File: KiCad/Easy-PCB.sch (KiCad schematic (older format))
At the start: 0 parts

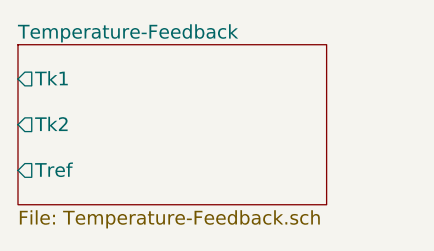
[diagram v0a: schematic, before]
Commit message: nichrome mounting parts added to bom and feedback terminal block removed
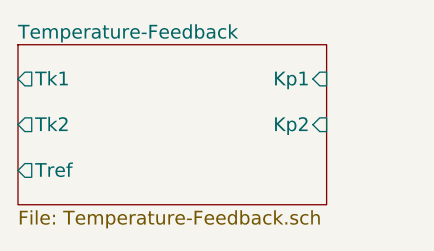
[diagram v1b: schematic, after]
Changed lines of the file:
@@
 F3 "Tk2" O L 4950 5600 60
 F4 "Tref" O L 4950 5800 60
+F5 "Kp1" I R 6300 5400 60
+F6 "Kp2" I R 6300 5600 60
 $EndSheet
 $EndSCHEMATC

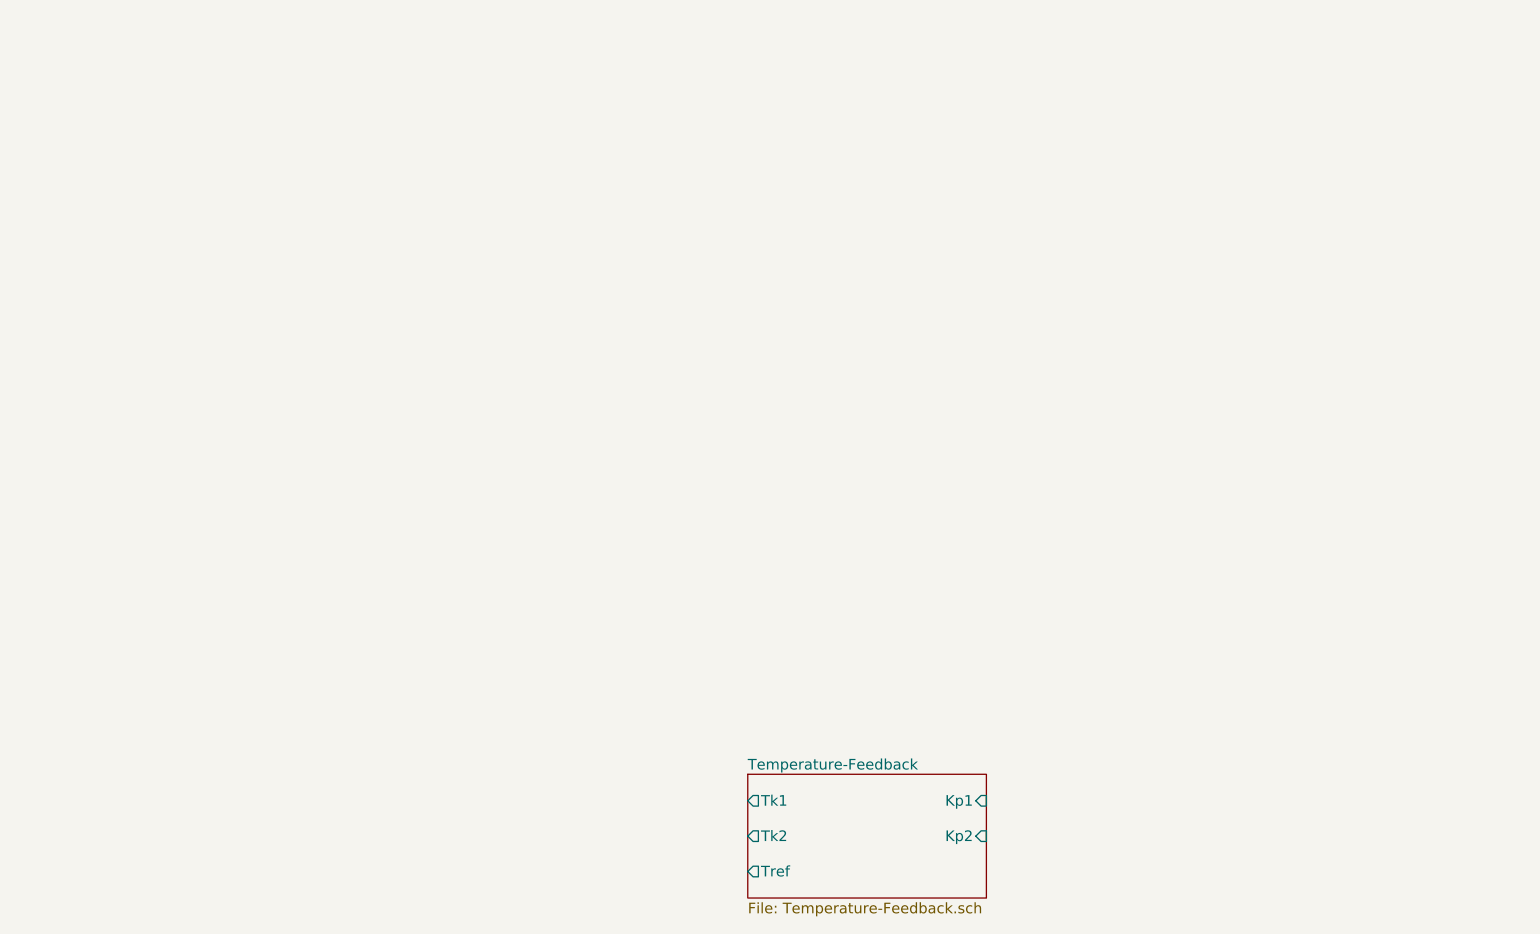
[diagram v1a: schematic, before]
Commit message: power circuit requirements section
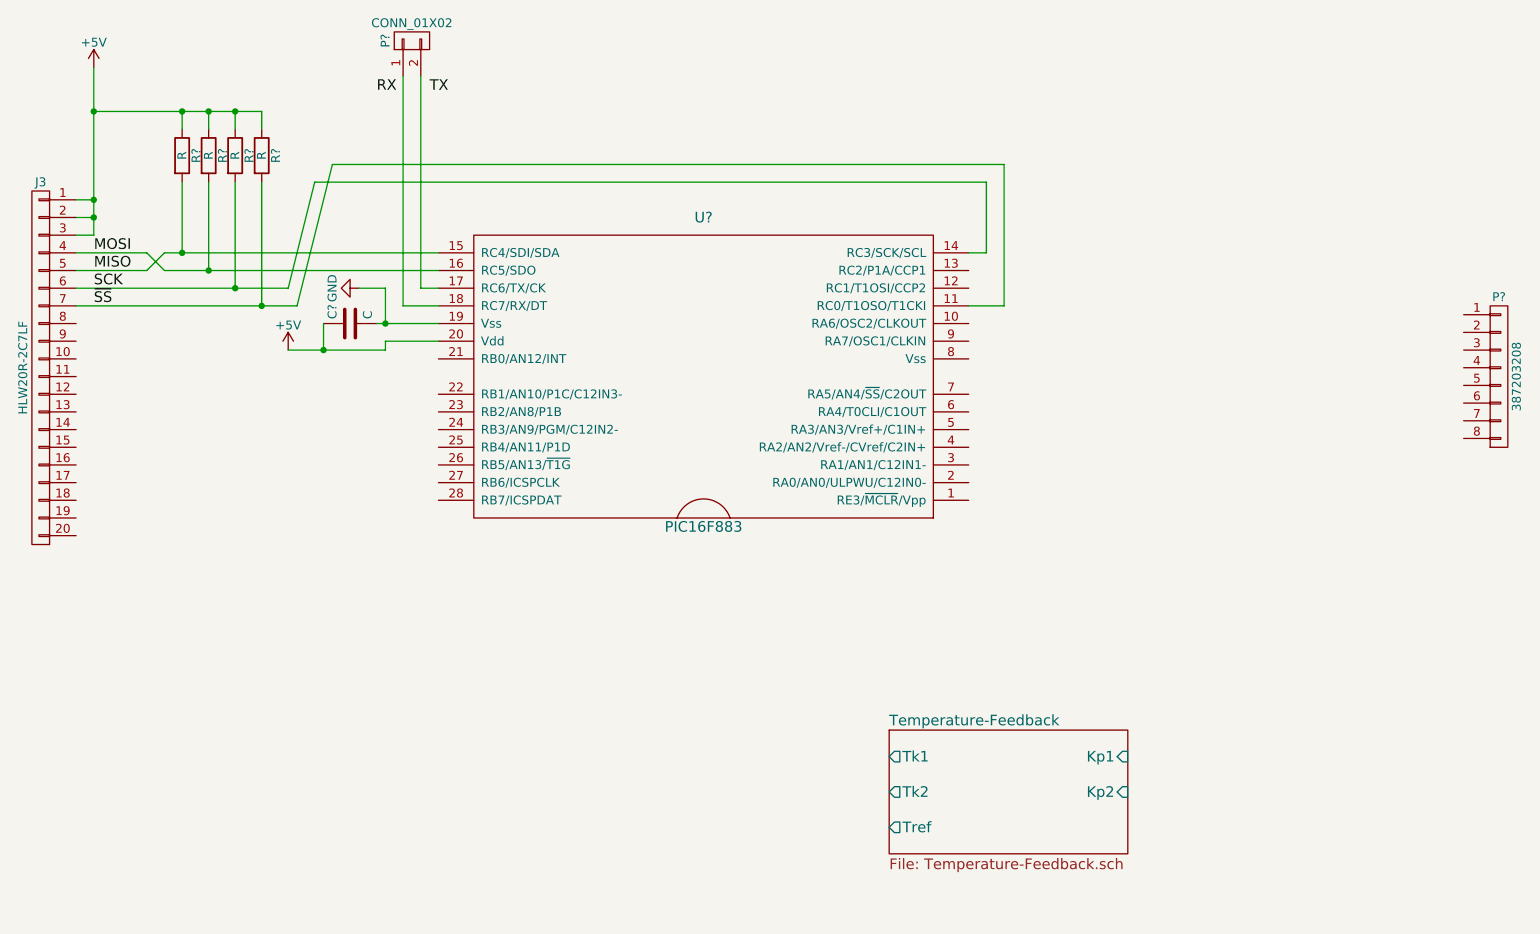
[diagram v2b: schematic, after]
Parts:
- added C?: C, symbol C
- added J3: HLW20R-2C7LF, symbol CONN_01X20
- added P?: 387203208, symbol CONN_01X08
- added P?: CONN_01X02, symbol CONN_01X02
- added R? (x4): R, symbol R
- added U?: PIC16F883, symbol PIC16F883
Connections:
- new net: P?.2 (P2), U?.17 (RC6/TX/CK)
- new net: P?.1 (P1), U?.18 (RC7/RX/DT)
- new net +5V: C?.1, J3.1 (P1), J3.2 (P2), J3.3 (P3), R?.1, R?.1, R?.1, R?.1, U?.20 (Vdd)
- new net GND: C?.2, U?.19 (Vss)
- new net MISO: J3.5 (P5), R?.2, U?.15 (RC4/SDI/SDA)
- new net MOSI: J3.4 (P4), R?.2, U?.16 (RC5/SDO)
- new net SCK: J3.6 (P6), R?.2, U?.14 (RC3/SCK/SCL)
- new net ~SS: J3.7 (P7), R?.2, U?.11 (RC0/T1OSO/T1CKI)

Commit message: updated temperature feedback schematic
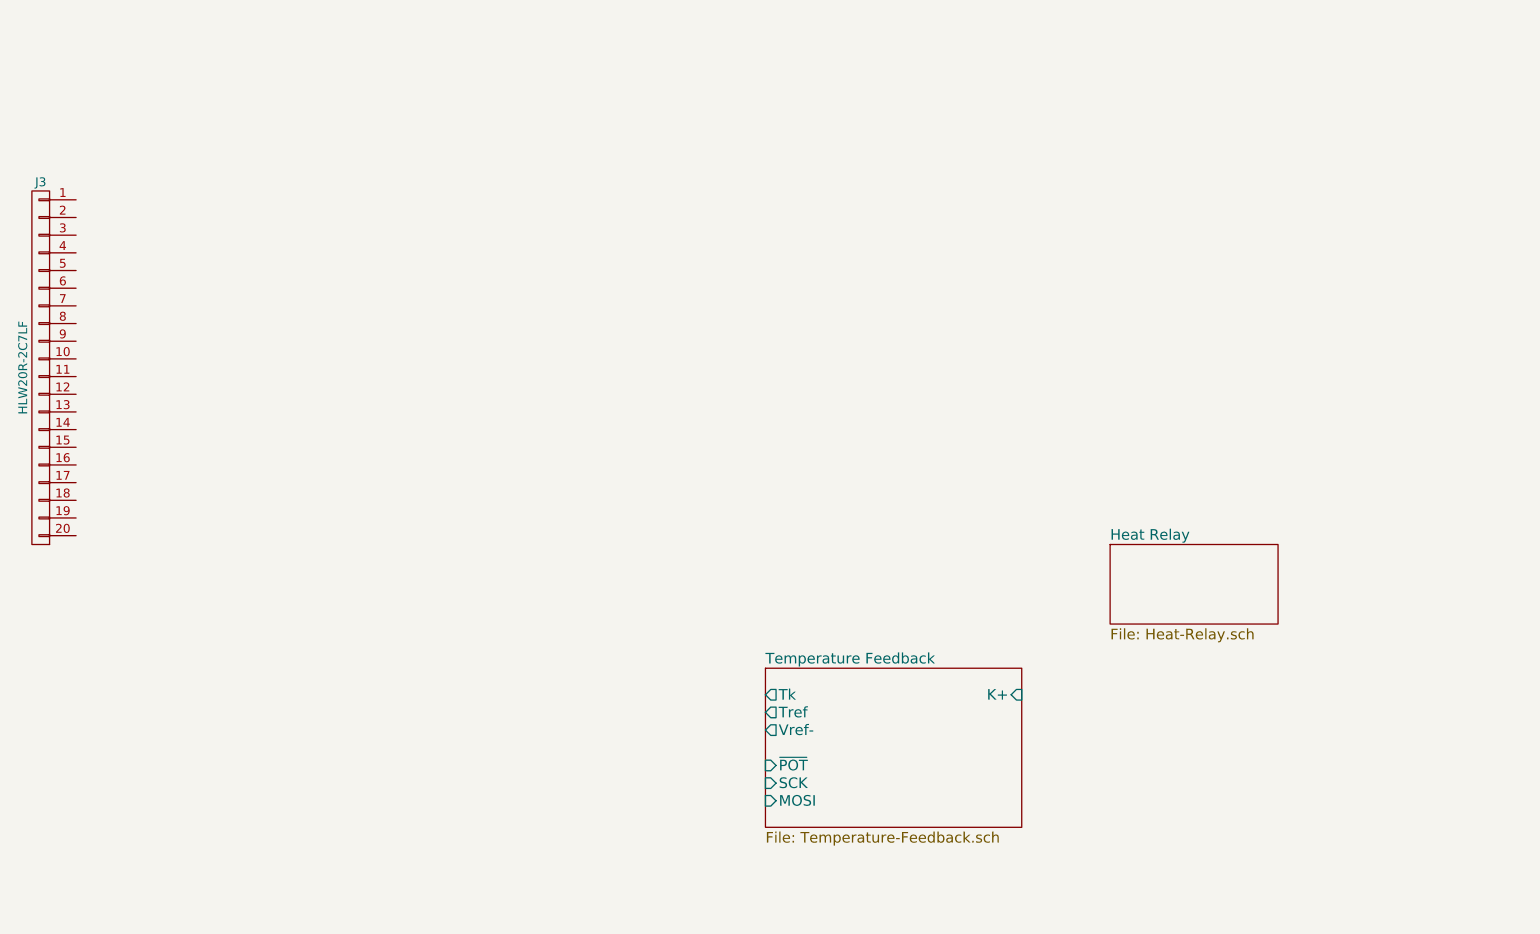
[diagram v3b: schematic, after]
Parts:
- removed C?: C, symbol C
- removed P?: 387203208, symbol CONN_01X08
- removed P?: CONN_01X02, symbol CONN_01X02
- removed R? (x4): R, symbol R
- removed U?: PIC16F883, symbol PIC16F883
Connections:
- removed net +5V: J3.1 (P1), J3.2 (P2), J3.3 (P3)
- net MISO: no longer names the net of J3.5 (P5)
- net MOSI: no longer names the net of J3.4 (P4)
- net SCK: no longer names the net of J3.6 (P6)
- net ~SS: no longer names the net of J3.7 (P7)
